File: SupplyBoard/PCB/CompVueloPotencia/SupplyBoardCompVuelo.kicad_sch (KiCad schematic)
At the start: 2 parts, among them J1 Conn_01x02, SW1 SW_SPDT

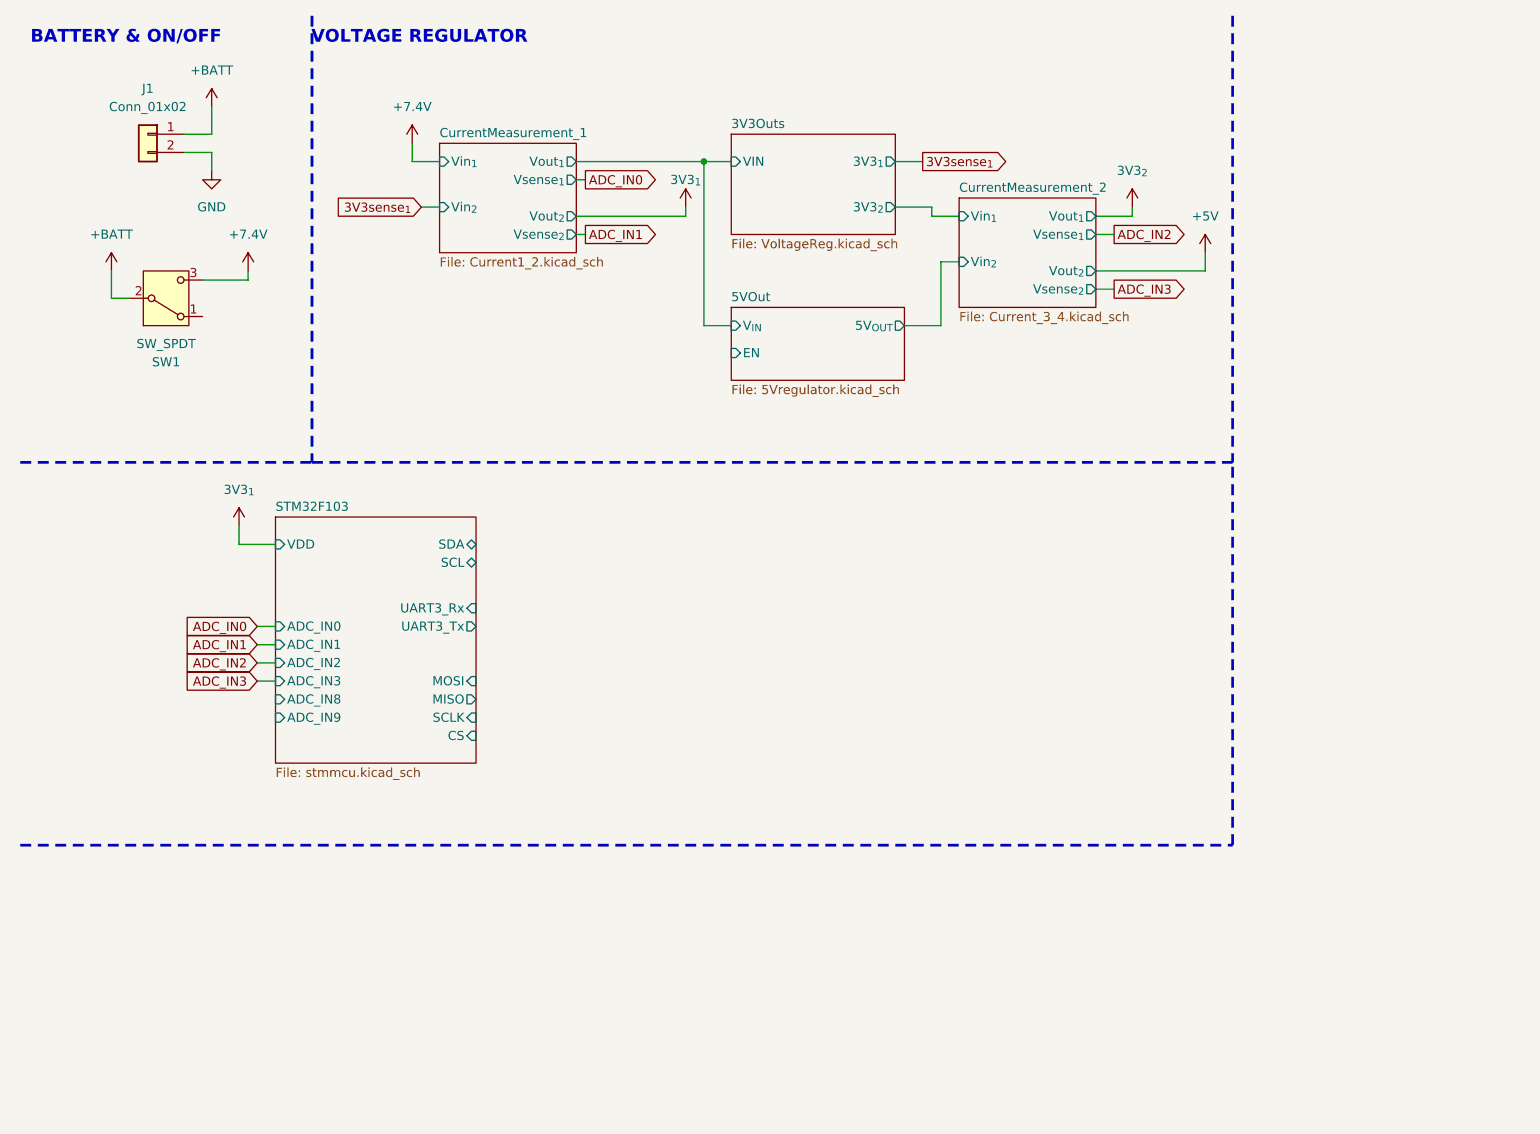
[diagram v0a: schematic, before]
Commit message: Supply board - Update the current measurement
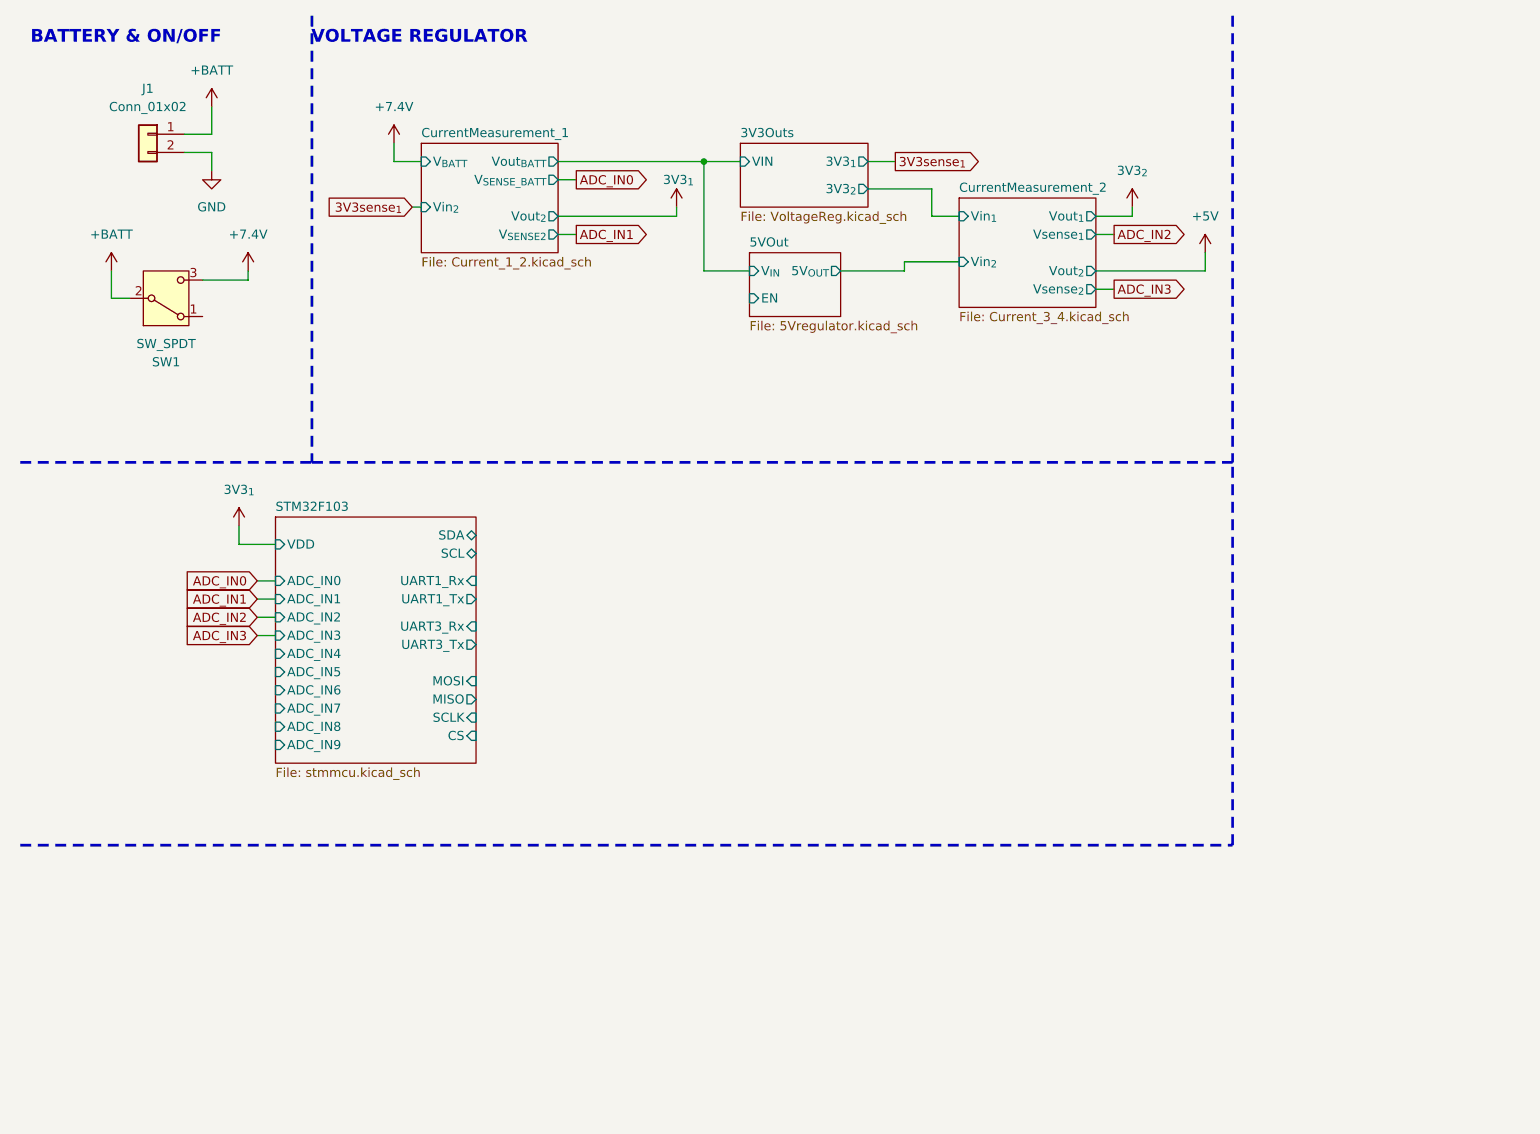
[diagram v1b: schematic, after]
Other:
- sheet CurrentMeasurement_1: file Current1_2.kicad_sch -> Current_1_2.kicad_sch
- sheet CurrentMeasurement_1 ports: added V_{BATT}, V_{SENSE2}, V_{SENSE_BATT}, Vout_{BATT}; removed Vin_{1}, Vout_{1}, Vsense_{1}, Vsense_{2}
- sheet STM32F103 ports: added ADC_IN4, ADC_IN5, ADC_IN6, ADC_IN7, UART1_Rx, UART1_Tx; removed none

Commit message: SupplyBoard - finish current sense
Finish the Current Sensor Circuit and add more 3.3V out, i change de microcontroles to a mcu that have the exact GPIO's
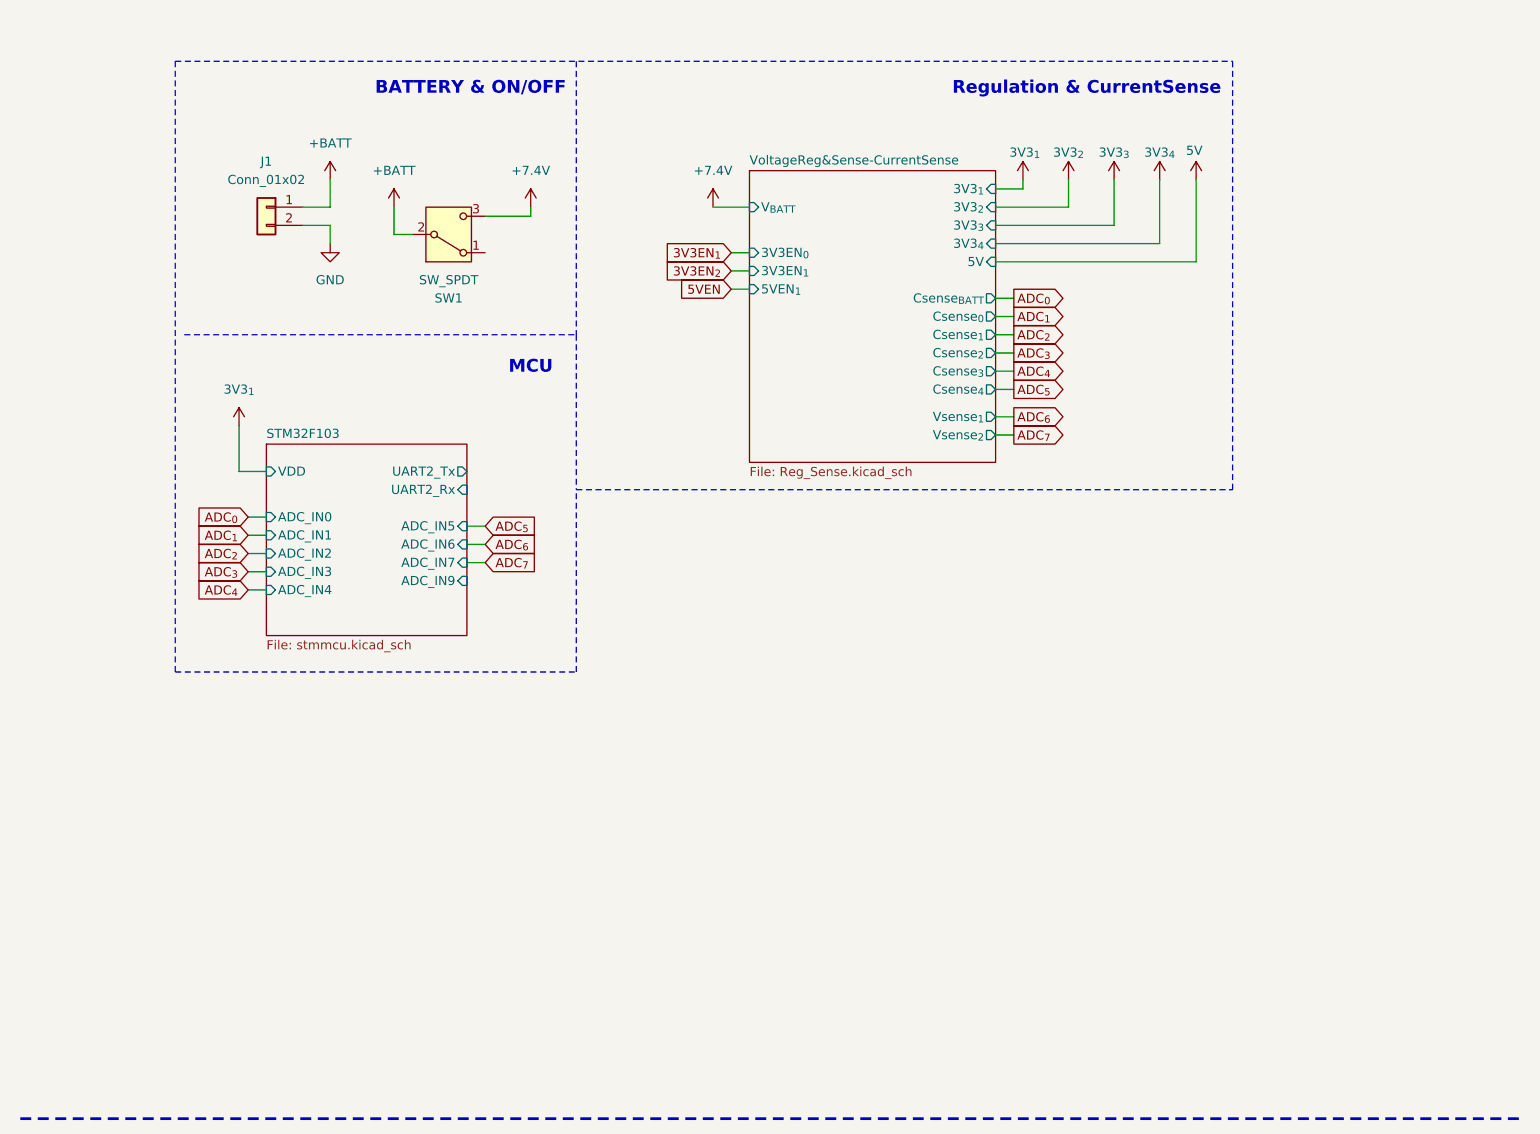
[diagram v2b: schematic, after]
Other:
- removed sheet 3V3Outs
- removed sheet 5VOut
- removed sheet CurrentMeasurement_1
- removed sheet CurrentMeasurement_2
- added sheet VoltageReg&Sense-CurrentSense (Reg_Sense.kicad_sch)
- sheet STM32F103 ports: added UART2_Rx, UART2_Tx; removed ADC_IN8, CS, MISO, MOSI, SCL, SCLK, SDA, UART1_Rx, UART1_Tx, UART3_Rx, UART3_Tx
- note added: "MCU"
- note added: "Regulation & CurrentSense"
- note removed: "VOLTAGE REGULATOR"
- moved on the sheet: J1, SW1

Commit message: SupplyBoard - update layout
schematic completed and PCB layout started; only the routing of the traces remains to be done
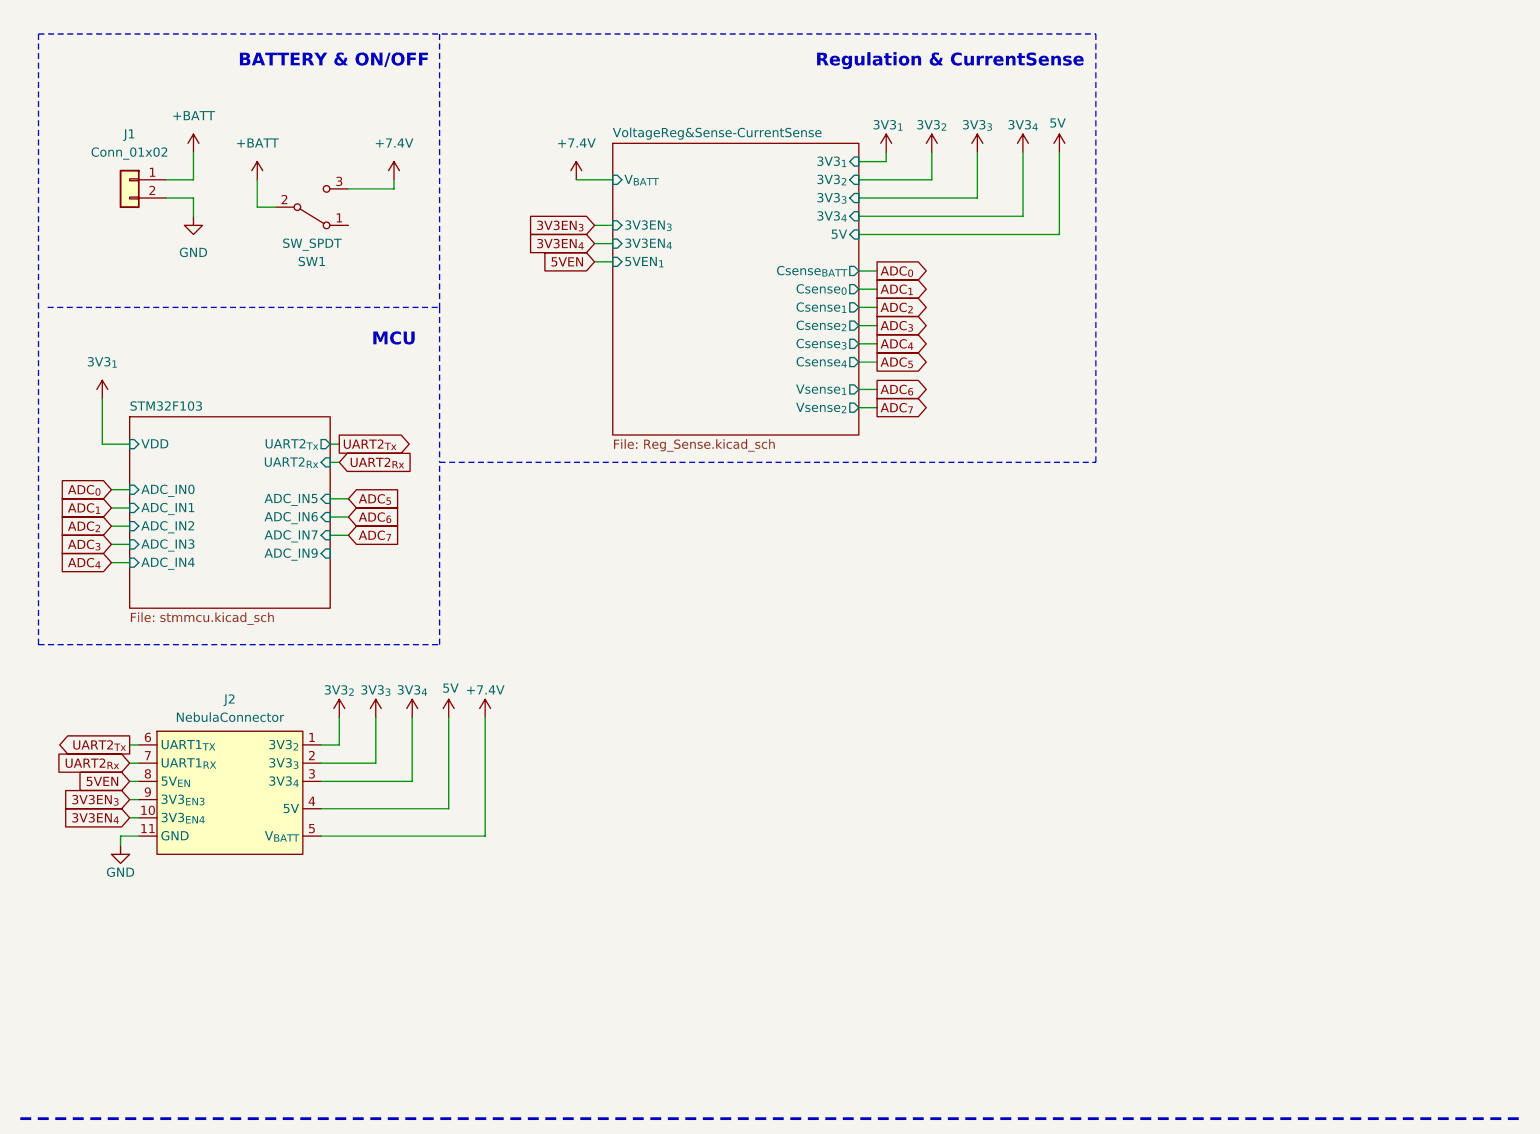
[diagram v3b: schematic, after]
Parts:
- removed SW1: SW_SPDT, symbol Switch:SW_SPDT
- added J2: NebulaConnector, CompVuelo:GeneralConn, symbol CompVuelo:GeneralConn
- added SW1: SW_SPDT, CompVuelo:SWSPDT, symbol CompVuelo:SW_SPDT
- J1: footprint Connector_AMASS:AMASS_XT60-M_1x02_P7.20mm_Vertical -> Connector_AMASS:AMASS_XT30U-F_1x02_P5.0mm_Vertical
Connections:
- net +7.4V: now also J2.5 (V_{BATT}), SW1.3
- net +BATT: now also SW1.2
- net 3V3_{2}: now also J2.1 (3V3_{2})
- net 3V3_{3}: now also J2.2 (3V3_{3})
- net 3V3_{4}: now also J2.3 (3V3_{4})
- net 5V: now also J2.4 (5V)
- net 5VEN: now also J2.8 (5V_{EN})
- net GND: now also J2.11 (GND)
- new net 3V3EN_{3}: J2.9 (3V3_{EN3})
- new net 3V3EN_{4}: J2.10 (3V3_{EN4})
- new net UART2_{Rx}: J2.7 (UART1_{RX})
- new net UART2_{Tx}: J2.6 (UART1_{TX})
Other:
- sheet STM32F103 ports: added UART2_{Rx}, UART2_{Tx}; removed UART2_Rx, UART2_Tx
- sheet VoltageReg&Sense-CurrentSense ports: added 3V3EN_{3}, 3V3EN_{4}; removed 3V3EN_{0}, 3V3EN_{1}
- moved on the sheet: J1
